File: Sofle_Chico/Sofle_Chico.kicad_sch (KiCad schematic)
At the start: 115 parts, among them J1 Conn_01x05, J2 MJ-4PP-9, J3 Conn_01x04, J4 Conn_01x04, J5 Conn_01x05, J6 Conn_01x05, J7 Conn_01x04, Q1 Si2301CDS, SW1 SW_PUSH, SW10 SW_PUSH, SW11 SW_PUSH, SW12 SW_PUSH, SW13 SW_PUSH, SW14 SW_PUSH, SW15 SW_PUSH, SW16 SW_PUSH, SW17 SW_PUSH, SW18 SW_PUSH, SW19 SW_PUSH, SW2 SW_PUSH, SW20 SW_PUSH, SW21 SW_PUSH, SW22 SW_PUSH, SW23 SW_PUSH, SW24 SW_PUSH, SW25 Rotary_Encoder_Switch-Device, SW26 SW_PUSH, SW27 SW_PUSH, SW28 SW_PUSH, SW29 SW_PUSH, SW3 SW_PUSH, SW30 SW_PUSH, SW4 SW_PUSH, SW5 SW_PUSH, SW6 SW_PUSH, SW7 SW_PUSH, SW8 SW_PUSH, SW9 SW_PUSH, U1 74LVC1G34SE-7, U2 Pico

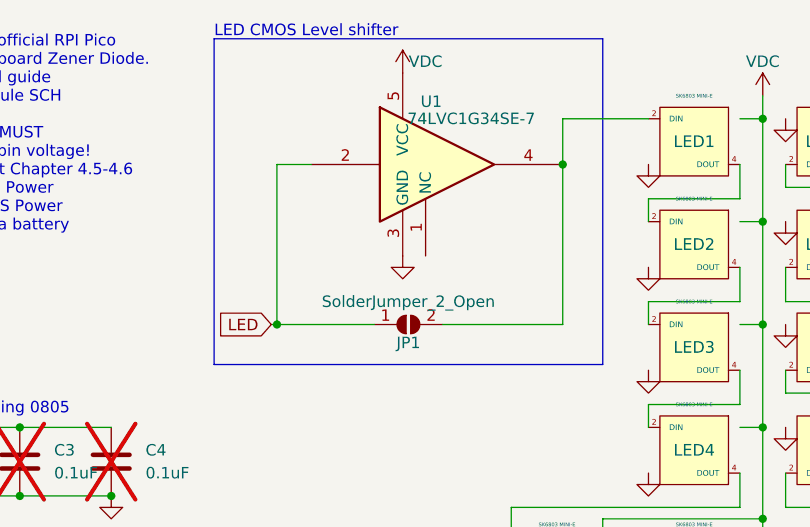
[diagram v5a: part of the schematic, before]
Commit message: Fixing accidentally misaligned switches/keycap 3d models
Removed level shifter from baseline design per Chico_panel prototype

Working on initial keyplate/cirque+oled 3d print designs
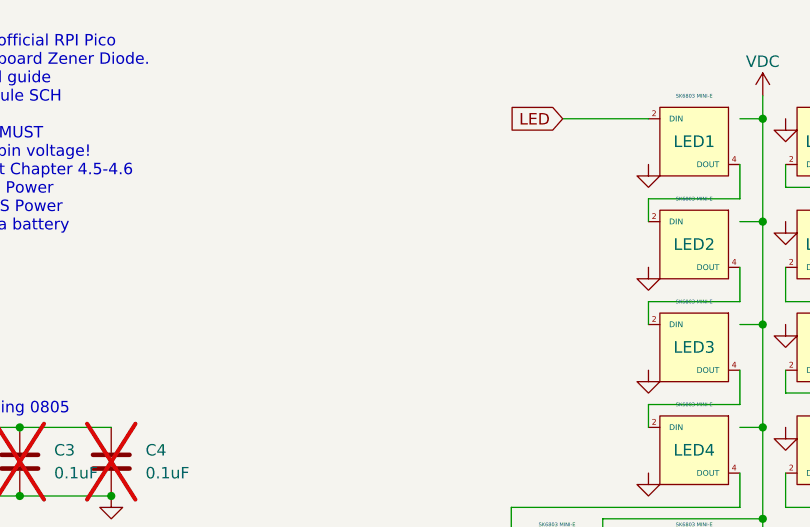
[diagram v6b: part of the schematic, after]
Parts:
- removed JP1: SolderJumper_2_Open, Sofle_Pico:Level Shifter Bypass Jumper, symbol Sofle_Pico:SolderJumper_2_Open
- removed U1: 74LVC1G34SE-7, Package_TO_SOT_SMD:SOT-353_SC-70-5_Handsoldering, symbol 74xGxx:74LVC1G34
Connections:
- net LED: now also LED1.2 (DIN)
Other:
- note removed: "LED CMOS Level shifter"
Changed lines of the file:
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@@
   (junction (at 204.47 123.19) (diameter 0) (color 0 0 0 0)
   )
-  (junction (at 133.985 48.26) (diameter 0) (color 0 0 0 0)
-  )
   (junction (at 215.9 59.69) (diameter 0) (color 0 0 0 0)
   )
@@
   (junction (at 240.03 114.3) (diameter 0) (color 0 0 0 0)
   )
-  (junction (at 165.735 30.48) (diameter 0) (color 0 0 0 0)
-  )
   (junction (at 143.51 139.7) (diameter 0) (color 0 0 0 0)
   )
@@
     (stroke (width 0) (type default))
   )
-  (wire (pts (xy 133.985 48.26) (xy 144.78 48.26))
-    (stroke (width 0) (type default))
-  )
   (wire (pts (xy 158.75 130.81) (xy 140.97 130.81))
     (stroke (width 0) (type default))
@@
     (stroke (width 0) (type default))
   )
-  (wire (pts (xy 133.985 30.48) (xy 133.985 48.26))
-    (stroke (width 0) (type default))
-  )
   (wire (pts (xy 218.44 55.88) (xy 218.44 53.34))
     (stroke (width 0) (type default))
@@
     (stroke (width 0) (type default))
   )
-  (wire (pts (xy 137.795 30.48) (xy 133.985 30.48))
-    (stroke (width 0) (type default))
-  )
   (wire (pts (xy 201.93 64.77) (xy 201.93 53.34))
     (stroke (width 0) (type default))
@@
     (stroke (width 0) (type default))
   )
-  (wire (pts (xy 165.735 30.48) (xy 165.735 48.26))
-    (stroke (width 0) (type default))
-  )
   (wire (pts (xy 185.42 45.72) (xy 175.26 45.72))
     (stroke (width 0) (type default))
@@
     (stroke (width 0) (type default))
   )
-  (wire (pts (xy 152.4 48.26) (xy 165.735 48.26))
-    (stroke (width 0) (type default))
-  )
   (wire (pts (xy 215.9 48.26) (xy 214.63 48.26))
     (stroke (width 0) (type default))
@@
     (stroke (width 0) (type default))
   )
-  (wire (pts (xy 133.985 48.26) (xy 133.35 48.26))
-    (stroke (width 0) (type default))
-  )
   (wire (pts (xy 187.96 69.85) (xy 187.96 73.025))
     (stroke (width 0) (type default))
@@
     (stroke (width 0) (type default))
   )
-  (wire (pts (xy 165.735 25.4) (xy 165.735 30.48))
-    (stroke (width 0) (type default))
-  )
   (wire (pts (xy 224.79 123.19) (xy 224.79 139.7))
     (stroke (width 0) (type default))
@@
     (fill (type none))
   )
-  (rectangle (start 127 16.51) (end 170.18 52.705)
-    (stroke (width 0) (type default))
-    (fill (type none))
-  )
   (rectangle (start 15.24 118.11) (end 62.23 142.24)
     (stroke (width 0) (type default))
@@
     (effects (font (size 1.27 1.27)) (justify left bottom))
   )
-  (text "LED CMOS Level shifter" (at 127 16.51 0)
-    (effects (font (size 1.27 1.27)) (justify left bottom))
-  )
   (text "OLEDs(Optional)\n" (at 15.24 88.9 0)
     (effects (font (size 1.27 1.27)) (justify left bottom))
@@
     )
   )
-  (global_label "LED" (shape input) (at 133.35 48.26 180) (fields_autoplaced)
+  (global_label "LED" (shape input) (at 165.735 25.4 180) (fields_autoplaced)
     (effects (font (size 1.27 1.27)) (justify right))
-    (property "Intersheetrefs" "${INTERSHEET_REFS}" (at 126.9971 48.26 0)
+    (property "Intersheetrefs" "${INTERSHEET_REFS}" (at 159.3821 25.4 0)
       (effects (font (size 1.27 1.27)) (justify right) hide)
     )
@@
     )
   )
-  (symbol (lib_id "74xGxx:74LVC1G34") (at 153.035 30.48 0) (unit 1)
-    (in_bom yes) (on_board yes) (dnp no)
-    (property "Reference" "U1" (at 151.13 23.495 0)
-      (effects (font (size 1.27 1.27)))
-    )
-    (property "Value" "74LVC1G34SE-7" (at 155.575 25.4 0)
-      (effects (font (size 1.27 1.27)))
-    )
-    (property "Footprint" "Package_TO_SOT_SMD:SOT-353_SC-70-5_Handsoldering" (at 153.035 30.48 0)
-      (effects (font (size 1.27 1.27)) hide)
-    )
-    (property "Datasheet" "https://www.diodes.com/assets/Datasheets/74LVC1G34.pdf" (at 153.035 30.48 0)
-      (effects (font (size 1.27 1.27)) hide)
-    )
-    (property "Mfg" "Diodes Inc / TI" (at 153.035 30.48 0)
-      (effects (font (size 1.27 1.27)) hide)
-    )
-    (property "JLCPCB_PN" "" (at 153.035 30.48 0)
-      (effects (font (size 1.27 1.27)) hide)
-    )
-    (pin "5")
-    (pin "4")
-    (pin "2")
-    (pin "3")
-    (pin "1")
-    (instances
-      (project "Sofle_Chico"
-        (path "/06057b3a-55ab-4f4e-913e-2aeec5ff3587"
-          (reference "U1") (unit 1)
-        )
-      )
-    )
-  )
   (symbol (lib_name "GND_1") (lib_id "power:GND") (at 218.44 59.69 0) (unit 1)
     (in_bom yes) (on_board yes) (dnp no)
@@
     )
   )
-  (symbol (lib_name "VDC_5") (lib_id "power:VDC") (at 147.955 20.32 0) (unit 1)
-    (in_bom yes) (on_board yes) (dnp no) (fields_autoplaced)
-    (property "Reference" "#PWR0110" (at 147.955 24.13 0)
-      (effects (font (size 1.27 1.27)) hide)
-    )
-    (property "Value" "VDC" (at 150.495 19.05 0)
-      (effects (font (size 1.27 1.27)))
-    )
-    (property "Footprint" "" (at 147.955 20.32 0)
-      (effects (font (size 1.27 1.27)) hide)
-    )
-    (property "Datasheet" "" (at 147.955 20.32 0)
-      (effects (font (size 1.27 1.27)) hide)
-    )
-    (pin "1")
-    (instances
-      (project "Sofle_Chico"
-        (path "/06057b3a-55ab-4f4e-913e-2aeec5ff3587"
-          (reference "#PWR0110") (unit 1)
-        )
-      )
-    )
-  )
   (symbol (lib_id "Sofle_Pico:SW_PUSH") (at 191.77 139.7 0) (unit 1)
     (in_bom yes) (on_board yes) (dnp no)
@@
     )
   )
-  (symbol (lib_id "Sofle_Pico:SolderJumper_2_Open") (at 148.59 48.26 0) (mirror x) (unit 1)
-    (in_bom yes) (on_board yes) (dnp no)
-    (property "Reference" "JP1" (at 148.59 50.292 0)
-      (effects (font (size 1.27 1.27)))
-    )
-    (property "Value" "SolderJumper_2_Open" (at 148.59 45.72 0)
-      (effects (font (size 1.27 1.27)))
-    )
-    (property "Footprint" "Sofle_Pico:Level Shifter Bypass Jumper" (at 148.59 48.26 0)
-      (effects (font (size 1.27 1.27)) hide)
-    )
-    (property "Datasheet" "~" (at 148.59 48.26 0)
-      (effects (font (size 1.27 1.27)) hide)
-    )
-    (property "JLCPCB_PN" "" (at 148.59 48.26 0)
-      (effects (font (size 1.27 1.27)) hide)
-    )
-    (pin "1")
-    (pin "2")
-    (instances
-      (project "Sofle_Chico"
-        (path "/06057b3a-55ab-4f4e-913e-2aeec5ff3587"
-          (reference "JP1") (unit 1)
-        )
-      )
-      (project "Junco"
-        (path "/c55ab6a7-e623-4136-bc89-8abb0d1fdb80"
-          (reference "JP1") (unit 1)
-        )
-      )
-    )
-  )
   (symbol (lib_name "SK6803MINIE_V2_1") (lib_id "Sofle_Pico:SK6803MINIE_V2") (at 237.49 39.37 0) (mirror y) (unit 1)
     (in_bom yes) (on_board yes) (dnp no)
@@
         )
       )
-    )
-  )
-  (symbol (lib_name "GND_6") (lib_id "power:GND") (at 147.955 40.64 0) (unit 1)
-    (in_bom yes) (on_board yes) (dnp no) (fields_autoplaced)
-    (property "Reference" "#PWR09" (at 147.955 46.99 0)
-      (effects (font (size 1.27 1.27)) hide)
-    )
-    (property "Value" "GND" (at 147.955 45.72 0)
-      (effects (font (size 1.27 1.27)) hide)
-    )
-    (property "Footprint" "" (at 147.955 40.64 0)
-      (effects (font (size 1.27 1.27)) hide)
-    )
-    (property "Datasheet" "" (at 147.955 40.64 0)
-      (effects (font (size 1.27 1.27)) hide)
-    )
-    (pin "1")
-    (instances
-      (project "Sofle_Chico"
-        (path "/06057b3a-55ab-4f4e-913e-2aeec5ff3587"
-          (reference "#PWR09") (unit 1)
-        )
-      )
-      (project "Sofle_v3"
-        (path "/aae4773e-62e9-4e6e-acb6-89e78a092249"
-          (reference "#PWR025") (unit 1)
-        )
-      )

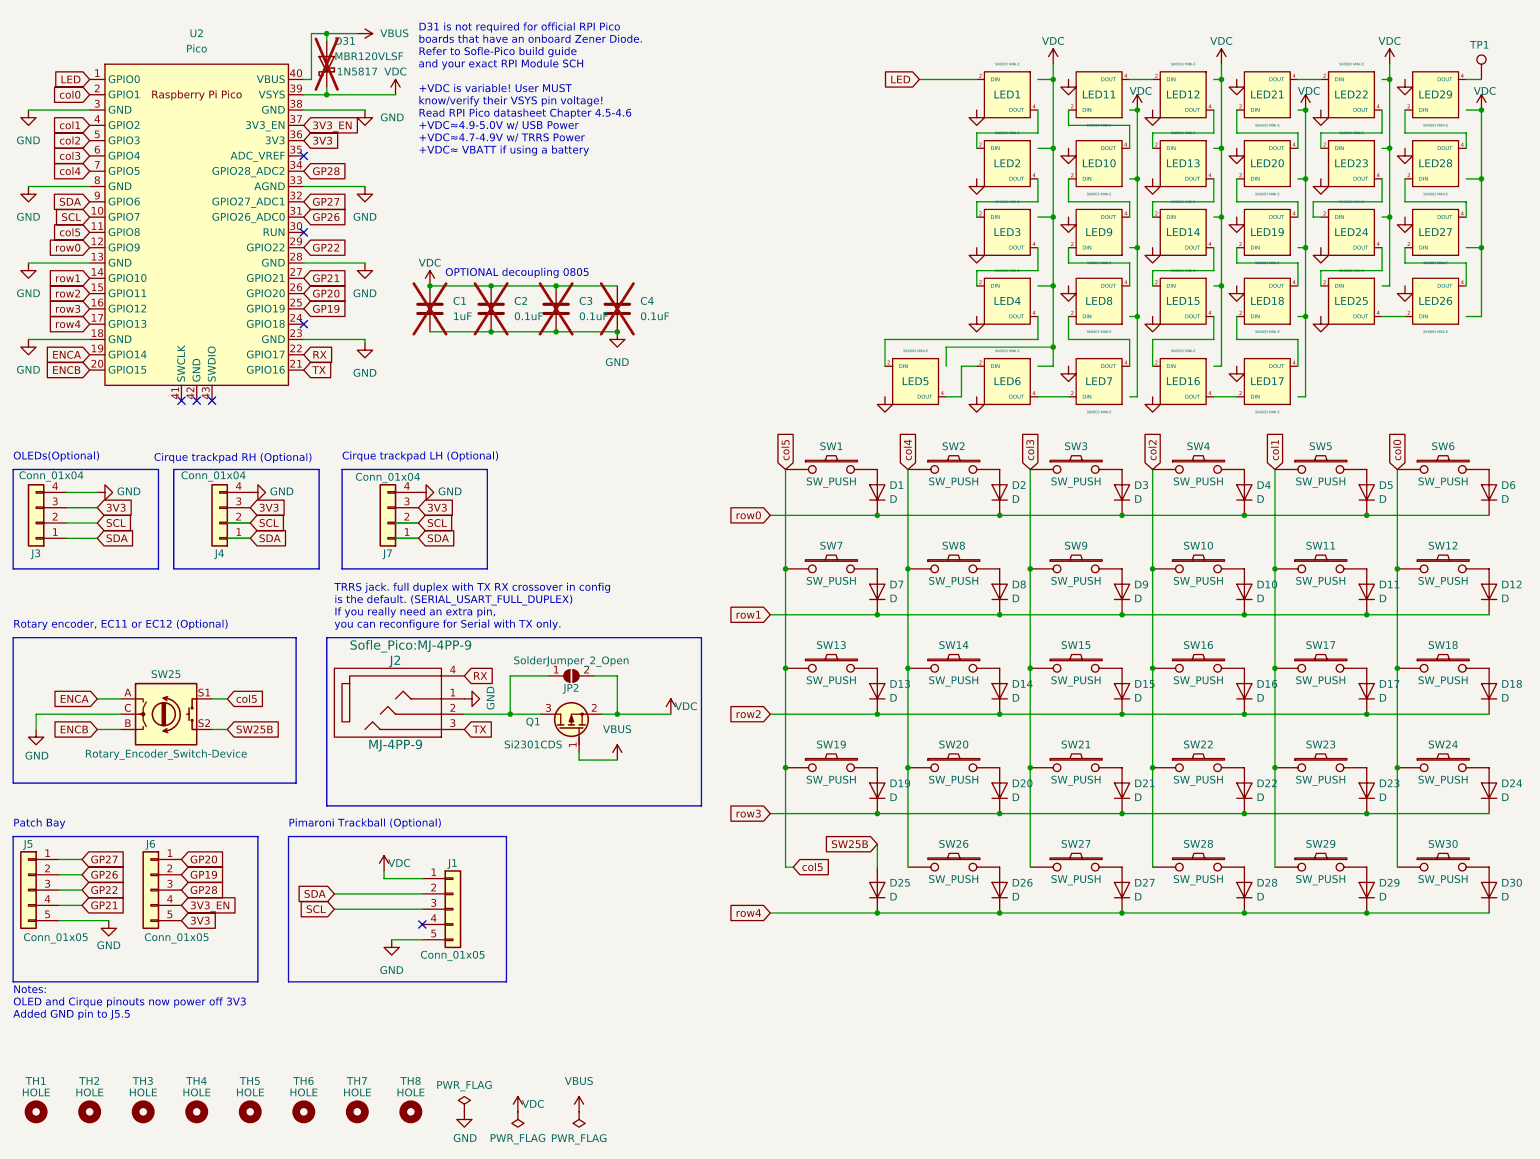
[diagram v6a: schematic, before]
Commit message: adding choc logos.
3.5.5 Work in Progress
Added I2C pullups under MCU
Added handedness resistors near patchbay
Patchbay reworked for 2x5 header and pinout optimized
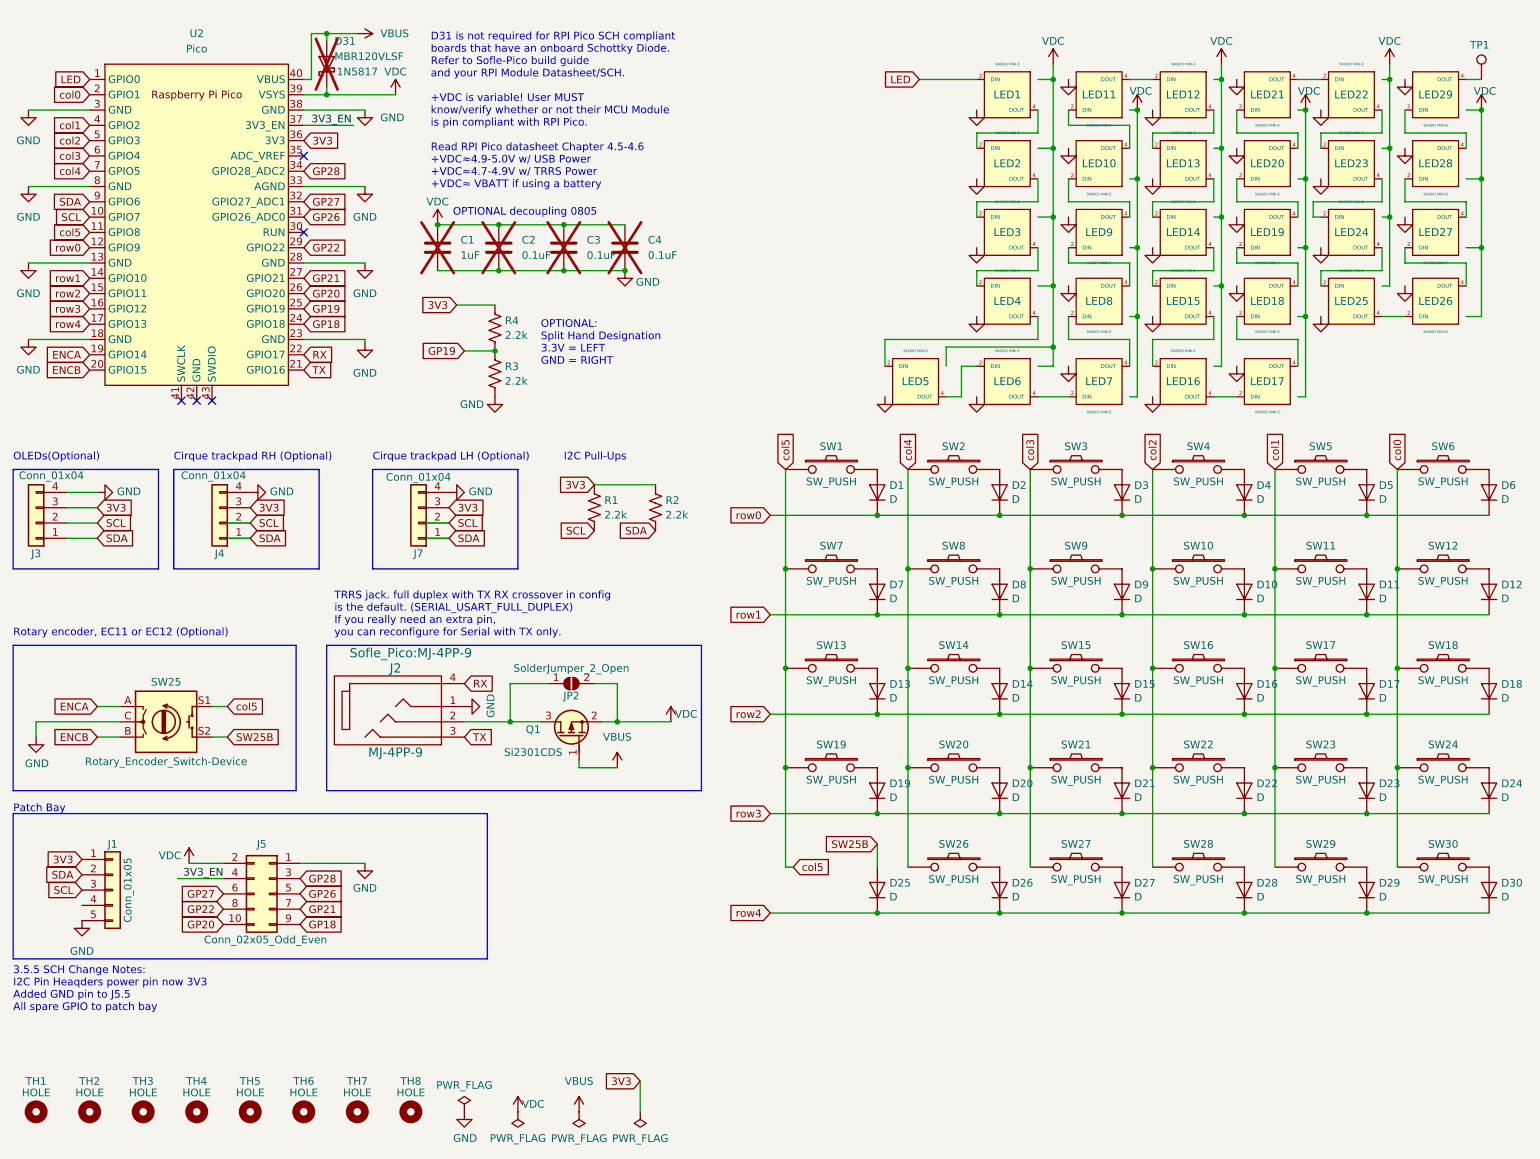
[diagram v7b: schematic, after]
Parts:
- removed J5, J6: Conn_01x05, Sofle_Pico:PinHeader_1x05_P2.54mm_Vertical, symbol Sofle_Pico:Conn_01x05
- added J5: Conn_02x05_Odd_Even, Connector_PinHeader_2.54mm:PinHeader_2x05_P2.54mm_Vertical, symbol Connector_Generic:Conn_02x05_Odd_Even
- added R1, R2, R3, R4: 2.2k, Sofle_Pico:Res_1206_SMD_6.3mm_TH_Hybrid, symbol Device:R_US
- Q1: footprint Sofle_Pico:SOT-23_DS -> Package_TO_SOT_SMD_AKL:SOT-23
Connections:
- net 3V3: now also J1.1 (Pin_1), R1.1, R2.1, R4.2
- net 3V3_EN: now also J5.4 (Pin_4)
- net GND: now also J5.1 (Pin_1), R3.2
- net GP19: now also R3.1, R4.1
- net GP20: now also J5.10 (Pin_10)
- net GP21: now also J5.7 (Pin_7)
- net GP22: now also J5.8 (Pin_8)
- net GP26: now also J5.5 (Pin_5)
- net GP27: now also J5.6 (Pin_6)
- net GP28: now also J5.3 (Pin_3)
- net SCL: now also R1.2
- net SDA: now also R2.2
- net VDC: now also J5.2 (Pin_2); no longer J1.1 (Pin_1)
- net GP18: now reaches U2.24 (GPIO18)
- net GP18: now also J5.9 (Pin_9)
- no-connect marks 7 -> 5
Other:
- note added: "3.5.5 SCH Change Notes: I2C Pin Heaqders power pin now 3V3 Added GND pin to J5.5 All spare GPIO to patch bay"
- note added: "D31 is not required for RPI Pico SCH compliant boards that have an onboard Schottky Diode. Refer to Sofle-Pico build guide and your RPI Module Datasheet/SCH. +VDC is variable! User MUST know/verify whether or not their MCU Module is pin compliant with RPI Pico. Read RPI Pico datasheet Chapter 4.5-4.6 +VDC≈4.9-5.0V w/ USB Power +VDC≈4.7-4.9V w/ TRRS Power +VDC≈ VBATT if using a battery"
- note added: "I2C Pull-Ups"
- note added: "OPTIONAL: Split Hand Designation 3.3V = LEFT GND = RIGHT"
- note removed: "D31 is not required for official RPI Pico boards that have an onboard Zener Diode. Refer to Sofle-Pico build guide and your exact RPI Module SCH +VDC is variable! User MUST know/verify their VSYS pin voltage! Read RPI Pico datasheet Chapter 4.5-4.6 +VDC≈4.9-5.0V w/ USB Power +VDC≈4.7-4.9V w/ TRRS Power +VDC≈ VBATT if using a battery"
- note removed: "Notes: OLED and Cirque pinouts now power off 3V3 Added GND pin to J5.5"
- note removed: "Pimaroni Trackball (Optional)"
- moved on the sheet: C1, C2, C3, C4, J1, J2, J7, JP2, Q1, SW25
